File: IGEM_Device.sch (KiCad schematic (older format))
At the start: 28 parts, among them J1 67997-410HLF, J2 Electrode_Conn, J3 Batt_Conn, SW1 Power_Switch, U1 SaBLE-X-R2, U2 TC1014-2.85VCT713, U3 LMP91000SD_NOPB, U4 LM334MX_NOPB, U5 TPS79718QDCKRQ1, U6 G-NIMO-003

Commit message: Update to PCB and Gerber files
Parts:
- gave numbers to parts that had none: 1
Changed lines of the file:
@@
 Connection ~ 2500 4050
 $Comp
-L 1N4148WT:1N4148WT D?
+L 1N4148WT:1N4148WT D1
 U 1 1 5D165C8E
 P 4700 1100
-F 0 "D?" H 4700 883 50  0000 C CNN
+F 0 "D1" H 4700 883 50  0000 C CNN
 F 1 "1N4148WT" H 4700 974 50  0000 C CNN
 F 2 "SODFL1608X70N" H 4700 1100 50  0001 L BNN

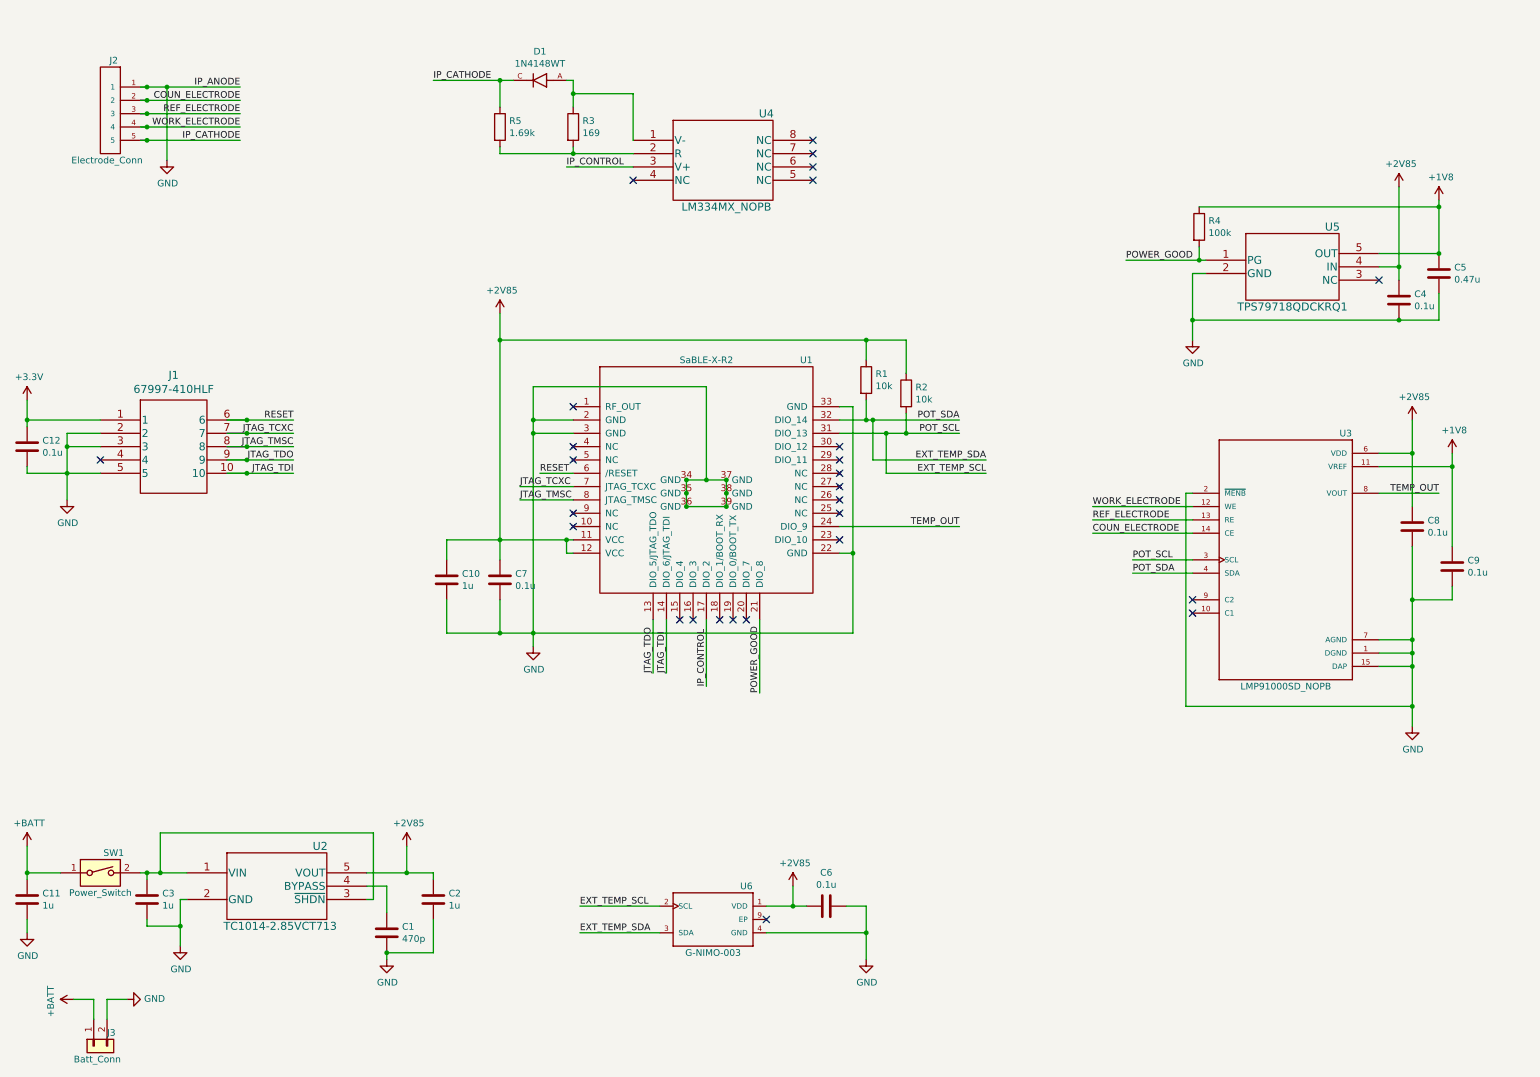
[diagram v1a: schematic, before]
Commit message: Added ADC
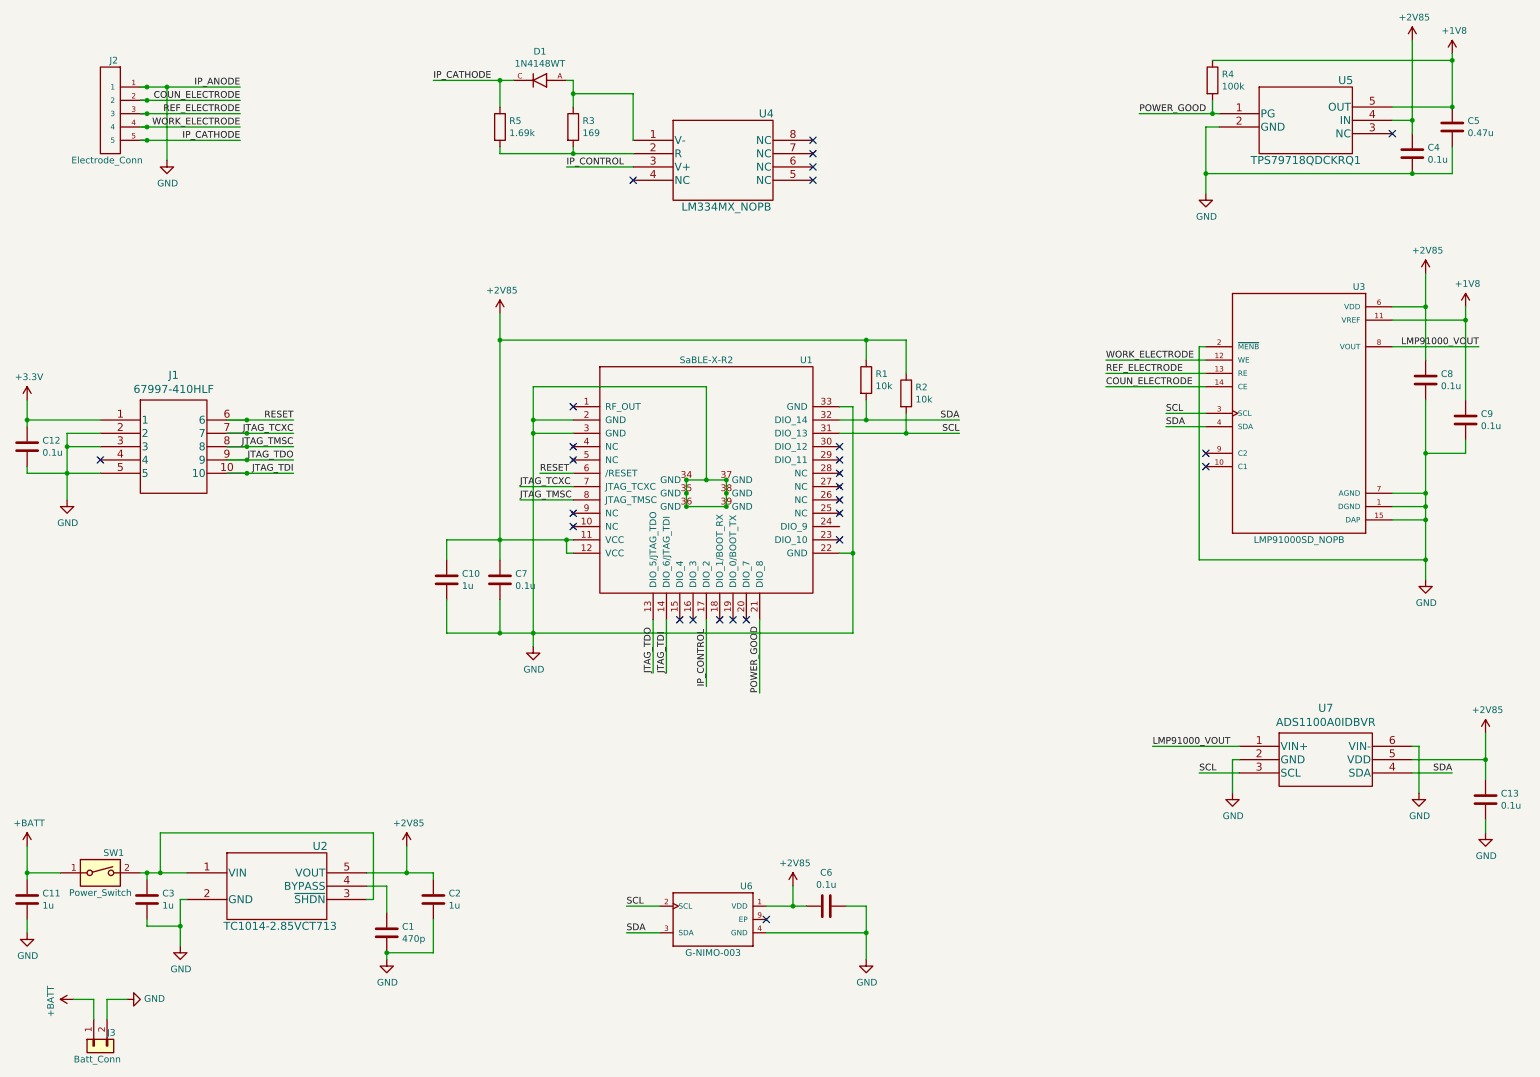
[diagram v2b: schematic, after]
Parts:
- added C13: 0.1u, symbol Device:C
- added U7: ADS1100A0IDBVR, DBV6, symbol IGEM_Device:ADS1100A0IDBVR
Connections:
- net labels added: LMP91000_VOUT, SCL, SDA
- net labels removed: EXT_TEMP_SCL, EXT_TEMP_SDA, POT_SCL, POT_SDA, TEMP_OUT
- wire segments 184 -> 188
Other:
- moved on the sheet: C4, C5, C8, C9, R4, U3, U5

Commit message: Minor fixes
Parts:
- removed C12, C9: 0.1u, Capacitors_SMD:C_0805, symbol Device:C
- removed J1: 67997-410HLF, footprints3:67997-410HLF, symbol 2019-05-30_20-01-46:67997-410HLF
- removed SW1: Power_Switch, footprints5:JS202011SCQN, symbol Switch:SW_DIP_x01
- added C13: 100p, Capacitors_SMD:C_0805, symbol Device:C
- added J1: M20-9980445, M20-9980445:HDRV8W64P254_2X4_1016X508X910P, symbol IGEM_Device:M20-9980445
- added J4: Male_Data_Conn, HTSW10407GS:HTSW-104-07-G-S, symbol Connector_Generic:Conn_01x04
- added J5: Female_Data_Conn, 55342372:5-534237-2, symbol Connector_Generic:Conn_01x04
- added J6: VDD_Female_Conn, 55342371:5-534237-1, symbol Connector_Generic:Conn_01x03
- added J7: GND_Female_Conn, 55342371:5-534237-1, symbol Connector_Generic:Conn_01x03
- added J8: VDD_Male_Conn, 51462803:5-146280-3, symbol Connector_Generic:Conn_01x03
- added J9: GND_Male_Conn, 51462803:5-146280-3, symbol Connector_Generic:Conn_01x03
- C12: renamed from C13; footprint (none) -> Capacitors_SMD:C_0805
- D1: footprint SODFL1608X70N -> 1N4148WT:SODFL1608X70N
- J3: footprint footprints6:796136-1 -> S2B-PH-K-S_LF__SN_:JST_S2B-PH-K-S(LF)(SN)
- U7: footprint DBV6 -> ADS1100A0TDBVR:ADS1100A0IDBVR
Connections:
- net labels removed: +3.3V
- wire segments 188 -> 210

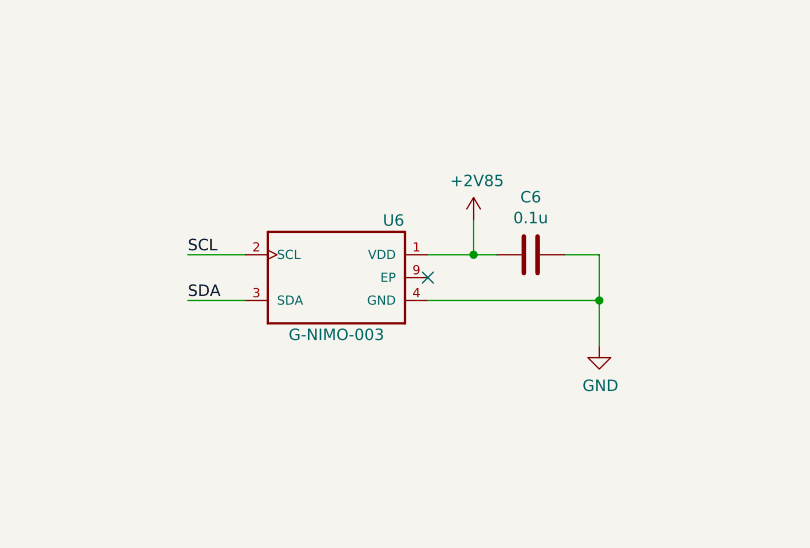
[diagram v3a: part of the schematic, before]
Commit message: Updated layout, added 3D shapes and Gerber files
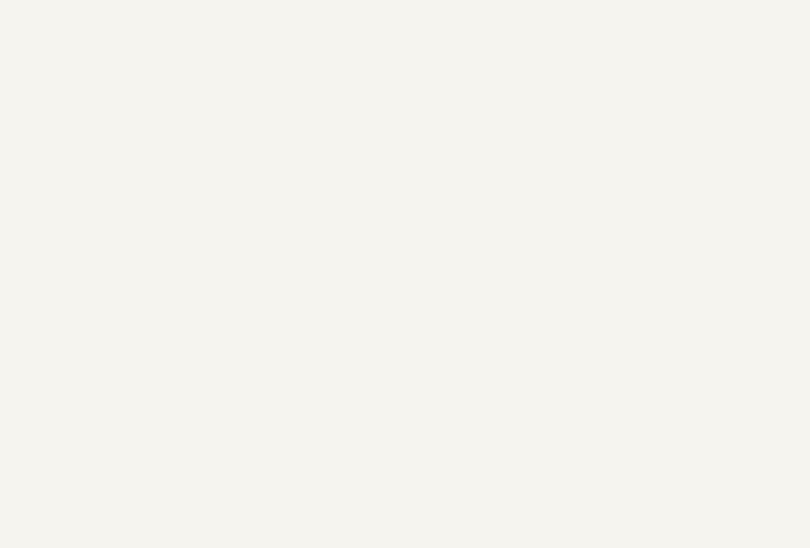
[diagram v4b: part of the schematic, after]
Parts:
- removed C6: 0.1u, Capacitors_SMD:C_0805, symbol Device:C
- removed U6: G-NIMO-003, G-NIMO-003:SON50P250X250X75-9N, symbol IGEM_Device:G-NIMO-003
- J2: footprint TSM-105-01-L-SH:TSM-105-01-L-SH -> TSW10508FSRA:TSW-105-08-F-S-RA
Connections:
- no-connect marks 27 -> 26
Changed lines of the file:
@@
 Wire Wire Line
 	2450 1250 1750 1250
-$Comp
-L IGEM_Device:G-NIMO-003 U6
-U 1 1 5D04021C
-P 6000 7400
-F 0 "U6" H 6250 7650 50  0000 C CNN
-F 1 "G-NIMO-003" H 6000 7150 50  0000 C CNN
-F 2 "G-NIMO-003:SON50P250X250X75-9N" H 6000 7400 50  0001 L BNN
-F 3 "G-NIMO-003" H 6000 7400 50  0001 L BNN
-F 4 "https://www.digikey.com/product-detail/en/te-connectivity-measurement-specialties/G-NIMO-003/223-1202-1-ND/4700925?utm_source=snapeda&utm_medium=aggregator&utm_campaign=symbol" H 6000 7400 50  0001 L BNN "Field4"
-F 5 "TE Connectivity" H 6000 7400 50  0001 L BNN "Field5"
-F 6 "TDFN-8 TE Connectivity" H 6000 7400 50  0001 L BNN "Field6"
-F 7 "TSYS02 Series 1.5 to 3.6 V Surface Mount Digital Temperature Sensor - TDFN-8" H 6000 7400 50  0001 L BNN "Field7"
-F 8 "G-NIMO-003" H 6000 7400 50  0001 L BNN "Field8"
-F 9 "223-1202-1-ND" H 6000 7400 50  0001 L BNN "Field9"
-F 10 "https://www.te.com/usa-en/product-G-NIMO-003.html?te_bu=Cor&te_type=disp&te_campaign=seda_glo_cor-seda-global-disp-prtnr-fy19-seda-model-bom-cta_sma-317_1&elqCampaignId=32493" H 6000 7400 50  0001 L BNN "Field10"
-	1    6000 7400
-	1    0    0    -1
-$EndComp
-$Comp
-L power:GND #PWR0115
-U 1 1 5D040377
-P 7150 7700
-F 0 "#PWR0115" H 7150 7450 50  0001 C CNN
-F 1 "GND" H 7155 7527 50  0000 C CNN
-F 2 "" H 7150 7700 50  0001 C CNN
-F 3 "" H 7150 7700 50  0001 C CNN
-	1    7150 7700
-	1    0    0    -1
-$EndComp
-$Comp
-L IGEM_Device:+2V85 #PWR0116
-U 1 1 5D0403CF
-P 6600 7150
-F 0 "#PWR0116" H 6600 7000 50  0001 C CNN
-F 1 "+2V85" H 6615 7323 50  0000 C CNN
-F 2 "" H 6600 7150 50  0001 C CNN
-F 3 "" H 6600 7150 50  0001 C CNN
-	1    6600 7150
-	1    0    0    -1
-$EndComp
-$Comp
-L Device:C C6
-U 1 1 5D04044D
-P 6850 7300
-F 0 "C6" V 6598 7300 50  0000 C CNN
-F 1 "0.1u" V 6689 7300 50  0000 C CNN
-F 2 "Capacitors_SMD:C_0805" H 6888 7150 50  0001 C CNN
-F 3 "~" H 6850 7300 50  0001 C CNN
-	1    6850 7300
-	0    1    1    0
-$EndComp
-Wire Wire Line
-	6400 7300 6600 7300
-Wire Wire Line
-	6600 7300 6600 7150
-Wire Wire Line
-	6700 7300 6600 7300
-Connection ~ 6600 7300
-Wire Wire Line
-	7000 7300 7150 7300
-Wire Wire Line
-	7150 7300 7150 7500
-Wire Wire Line
-	6400 7500 7150 7500
-Connection ~ 7150 7500
-Wire Wire Line
-	7150 7500 7150 7700
-Text Label 5350 7500 0    50   ~ 0
-SDA
-Text Label 5350 7300 0    50   ~ 0
-SCL
-NoConn ~ 6400 7400
 Wire Wire Line
 	2450 1550 1750 1550
@@
 F 0 "J2" H 1600 1350 50  0000 C CNN
 F 1 "Electrode_Conn" H 1650 600 50  0000 C CNN
-F 2 "TSM-105-01-L-SH:TSM-105-01-L-SH" H 1550 1150 50  0001 L BNN
+F 2 "TSW10508FSRA:TSW-105-08-F-S-RA" H 1550 1150 50  0001 L BNN
 F 3 "TSM-105-01-L-SH" H 1550 1150 50  0001 L BNN
 F 4 "SAM12229-ND" H 1550 1150 50  0001 L BNN "Field4"
@@
 	7150 3650 7850 3650
 Wire Wire Line
-	5600 7300 5350 7300
-Wire Wire Line
-	5600 7500 5350 7500
-Wire Wire Line
 	9700 3600 9400 3600
